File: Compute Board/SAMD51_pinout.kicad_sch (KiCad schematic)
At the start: 10 parts, among them U11 SAMD51

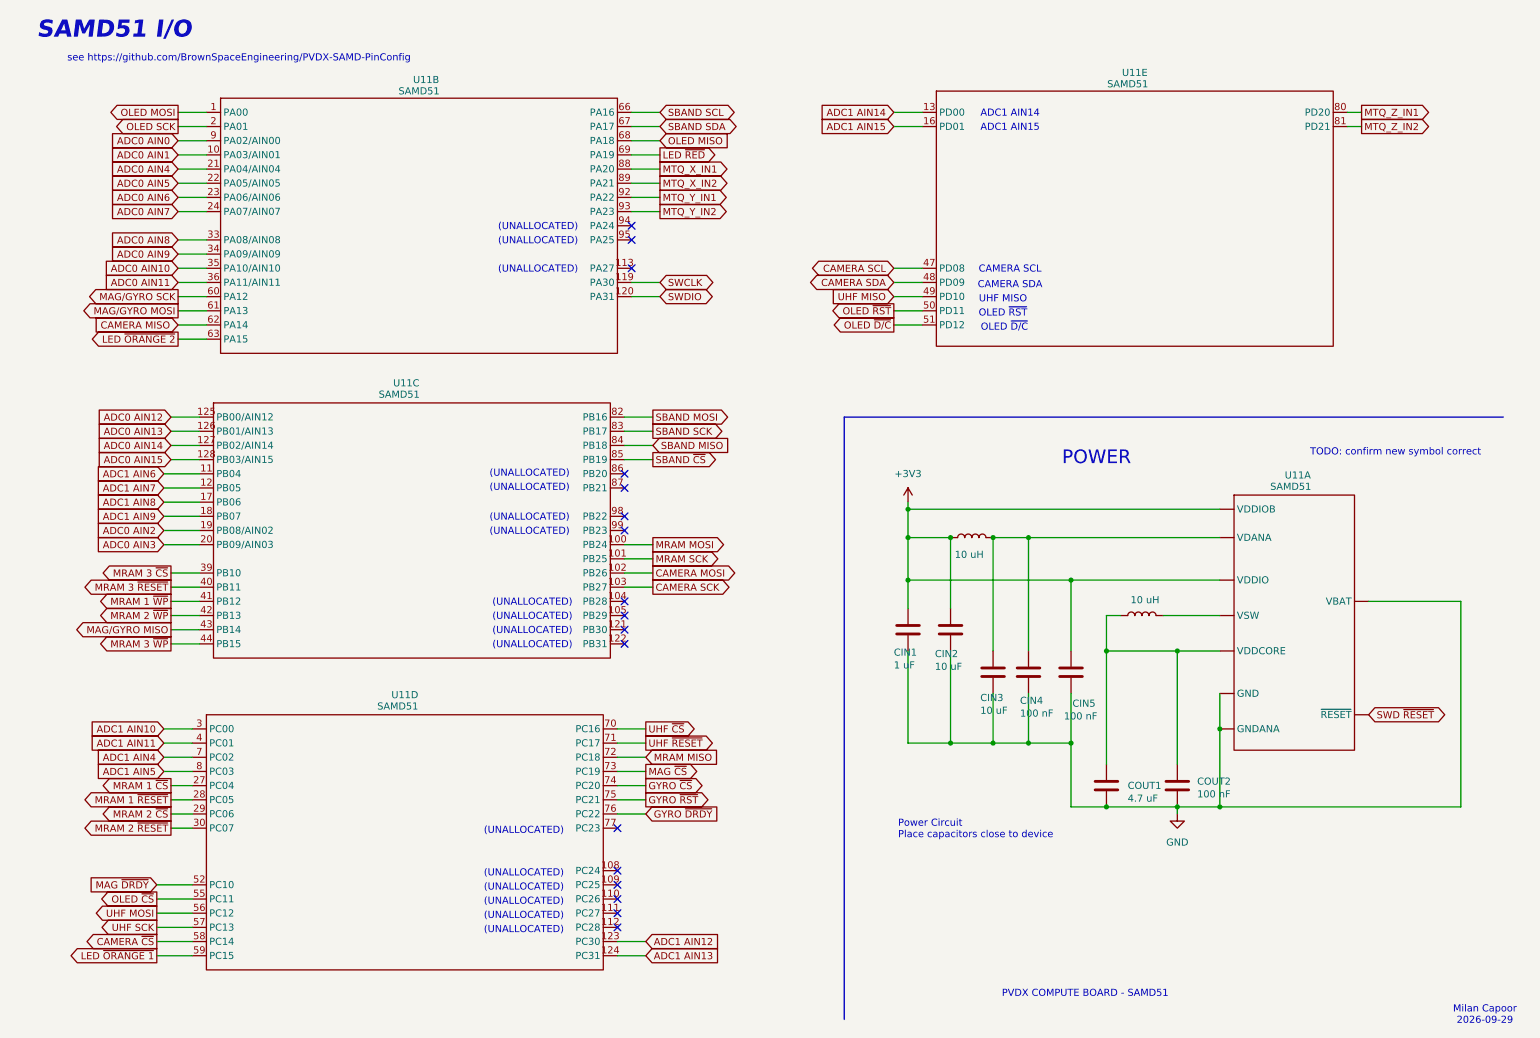
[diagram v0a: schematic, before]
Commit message: Push layout-ready schematics and partial routing
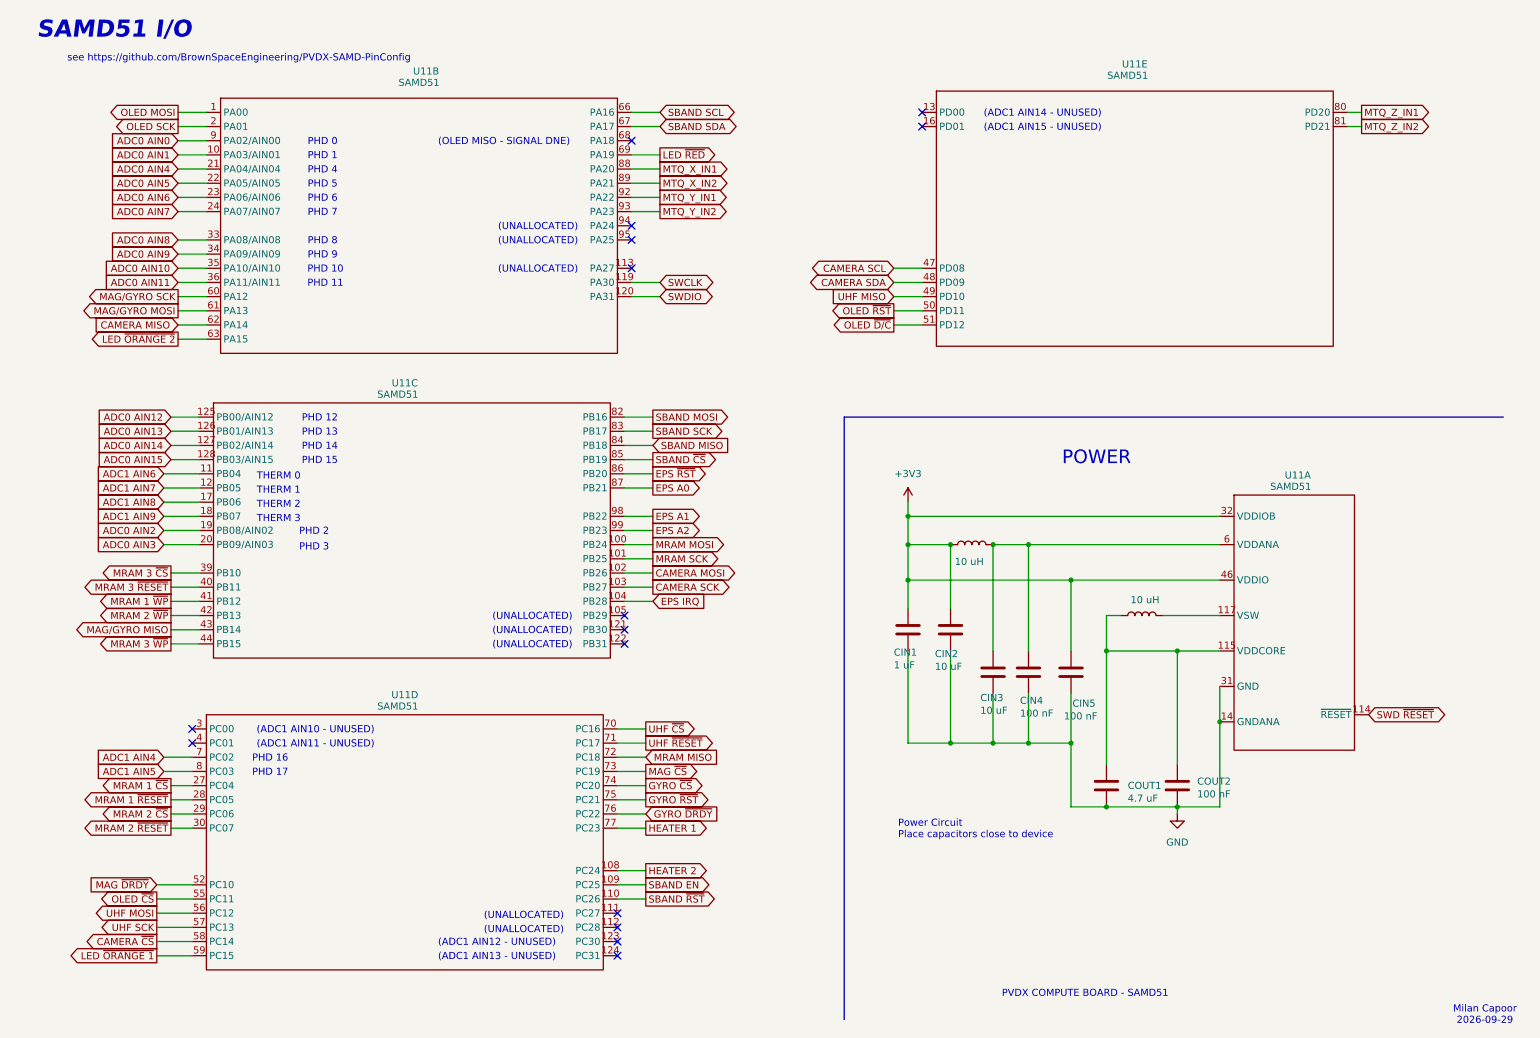
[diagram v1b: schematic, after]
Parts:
- CIN1, CIN2, CIN3, CIN4, CIN5, COUT1, COUT2: footprint Capacitor_SMD:C_0402_1005Metric -> Capacitor_SMD:C_0603_1608Metric
- L3, L4: footprint Inductor_SMD:L_0402_1005Metric -> Inductor_SMD:L_0603_1608Metric
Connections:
- net +3V3: now also U11.107 (VDDIO), U11.118 (VDDIO), U11.32 (VDDIOB), U11.37 (VDDIOB), U11.46 (VDDIO), U11.54 (VDDIO), U11.65 (VDDIO), U11.79 (VDDIO), U11.91 (VDDIO), U11.97 (VDDIO); no longer U11. (~{RESET})
- net GND: now also U11.106 (GND), U11.14 (GNDANA), U11.25 (GNDANA), U11.31 (GND), U11.38 (GND), U11.45 (GND), U11.5 (GND), U11.53 (GND), U11.64 (GND), U11.78 (GND), U11.90 (GND), U11.96 (GND); no longer U11. (~{RESET})
- net SWD ~{RESET}: now also U11.114 (~{RESET}); no longer U11. (~{RESET})
- net VDDANA: now reaches CIN3.1, CIN4.1, L3.2
- net VDDANA: now also U11.15 (VDDANA), U11.26 (VDDANA), U11.6 (VDDANA); no longer U11. (~{RESET})
- net at COUT1.1, COUT2.1, L4.1: now also U11.115 (VDDCORE); no longer U11. (~{RESET})
- net at L4.2: now also U11.117 (VSW); no longer U11. (~{RESET})
- net HEATER 2: now reaches U11.108 (PC24)
- net SBAND EN: now reaches U11.109 (PC25)
- net SBAND ~{RST}: now reaches U11.110 (PC26)
- net HEATER 1: now reaches U11.77 (PC23)
- net EPS IRQ: now reaches U11.104 (PB28)
- net EPS ~{RST}: now reaches U11.86 (PB20)
- net EPS A0: now reaches U11.87 (PB21)
- net EPS A1: now reaches U11.98 (PB22)
- net EPS A2: now reaches U11.99 (PB23)
- net ADC1 AIN10: no longer names the net of U11.3 (PC00)
- net ADC1 AIN11: no longer names the net of U11.4 (PC01)
- net ADC1 AIN12: no longer names the net of U11.123 (PC30)
- net ADC1 AIN13: no longer names the net of U11.124 (PC31)
- net ADC1 AIN14: no longer names the net of U11.13 (PD00)
- net ADC1 AIN15: no longer names the net of U11.16 (PD01)
- net OLED MISO: no longer names the net of U11.68 (PA18)
- no-connect marks 17 -> 15
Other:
- note added: "(ADC1 AIN10 - UNUSED)"
- note added: "(ADC1 AIN11 - UNUSED)"
- note added: "(ADC1 AIN12 - UNUSED)"
- note added: "(ADC1 AIN13 - UNUSED)"
- note added: "(ADC1 AIN14 - UNUSED)"
- note added: "(ADC1 AIN15 - UNUSED)"
- note added: "(OLED MISO - SIGNAL DNE)"
- note added: "PHD 0"
- note added: "PHD 1"
- note added: "PHD 10"
- note added: "PHD 11"
- note added: "PHD 12"
- note added: "PHD 13"
- note added: "PHD 14"
- note added: "PHD 15"
- note added: "PHD 16"
- note added: "PHD 17"
- note added: "PHD 2"
- note added: "PHD 3"
- note added: "PHD 4"
- note added: "PHD 5"
- note added: "PHD 6"
- note added: "PHD 7"
- note added: "PHD 8"
- note added: "PHD 9"
- note added: "THERM 0"
- note added: "THERM 1"
- note added: "THERM 2"
- note added: "THERM 3"
- note removed: "ADC1 AIN14"
- note removed: "ADC1 AIN15"
- note removed: "CAMERA SCL"
- note removed: "CAMERA SDA"
- note removed: "OLED ~{D/C}"
- note removed: "OLED ~{RST}"
- note removed: "TODO: confirm new symbol correct"
- note removed: "UHF MISO"

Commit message: Push finished layout minus perovskites
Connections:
- net GND: now also U11.116 (GNDIO)
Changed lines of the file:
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@@
+	)
+	(symbol
+		(lib_id "power:GND")
+		(at 256.54 134.62 90)
+		(unit 1)
+		(body_style 1)
+		(exclude_from_sim no)
+		(in_bom yes)
+		(on_board yes)
+		(in_pos_files yes)
+		(dnp no)
+		(fields_autoplaced yes)
+		(property "Reference" "#PWR065"
+			(at 262.89 134.62 0)
+			(hide yes)
+			(show_name no)
+			(do_not_autoplace no)
+			(effects
+				(font
+					(size 1.27 1.27)
+				)
+			)
+		)
+		(property "Value" "GND"
+			(at 260.35 134.6199 90)
+			(show_name no)
+			(do_not_autoplace no)
+			(effects
+				(font
+					(size 1.27 1.27)
+				)
+				(justify right)
+			)
+		)
+		(property "Footprint" ""
+			(at 256.54 134.62 0)
+			(hide yes)
+			(show_name no)
+			(do_not_autoplace no)
+			(effects
+				(font
+					(size 1.27 1.27)
+				)
+			)
+		)
+		(property "Datasheet" ""
+			(at 256.54 134.62 0)
+			(hide yes)
+			(show_name no)
+			(do_not_autoplace no)
+			(effects
+				(font
+					(size 1.27 1.27)
+				)
+			)
+		)
+		(property "Description" "Power symbol creates a global label with name \"GND\" , ground"
+			(at 256.54 134.62 0)
+			(hide yes)
+			(show_name no)
+			(do_not_autoplace no)
+			(effects
+				(font
+					(size 1.27 1.27)
+				)
+			)
+		)
+		(pin "1"
+		)
+		(instances
+			(project "PVDX Compute Board"
+				(path "/cc5055d2-349f-4e91-a151-9a2f788b119f/ea0f2518-2951-420b-9275-c672d5183aa9"
+					(reference "#PWR065")
+					(unit 1)
+				)
+			)
+		)
 	)
 	(symbol
@@
 		(pin "117"
 		)
+		(pin "116"
+		)
 		(instances
 			(project "PVDX Compute Board"
@@
 		(pin "117"
 		)
+		(pin "116"
+		)
 		(instances
 			(project "PVDX Compute Board"
@@
 		(pin "117"
 		)
+		(pin "116"
+		)
 		(instances
 			(project "PVDX Compute Board"
@@
 		(pin "117"
 		)
+		(pin "116"
+		)
 		(instances
 			(project "PVDX Compute Board"
@@
 		(pin "117"
 		)
+		(pin "116"
+		)
 		(instances

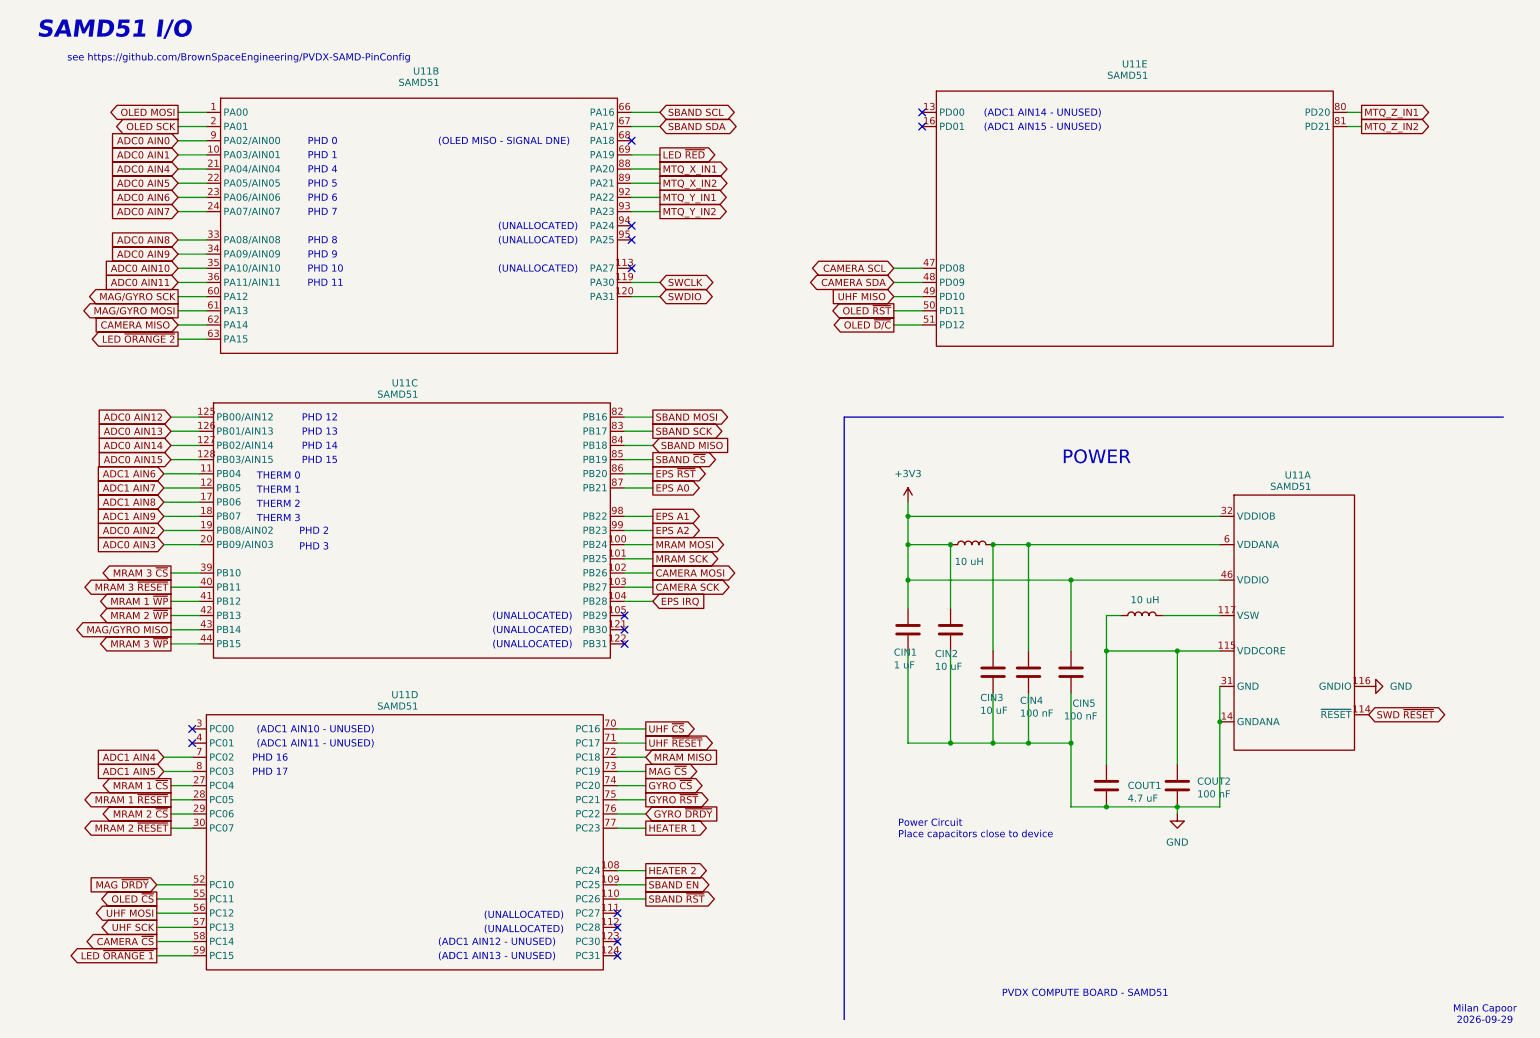
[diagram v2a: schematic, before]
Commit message: Add perovskite and magnetorquer sleep routing
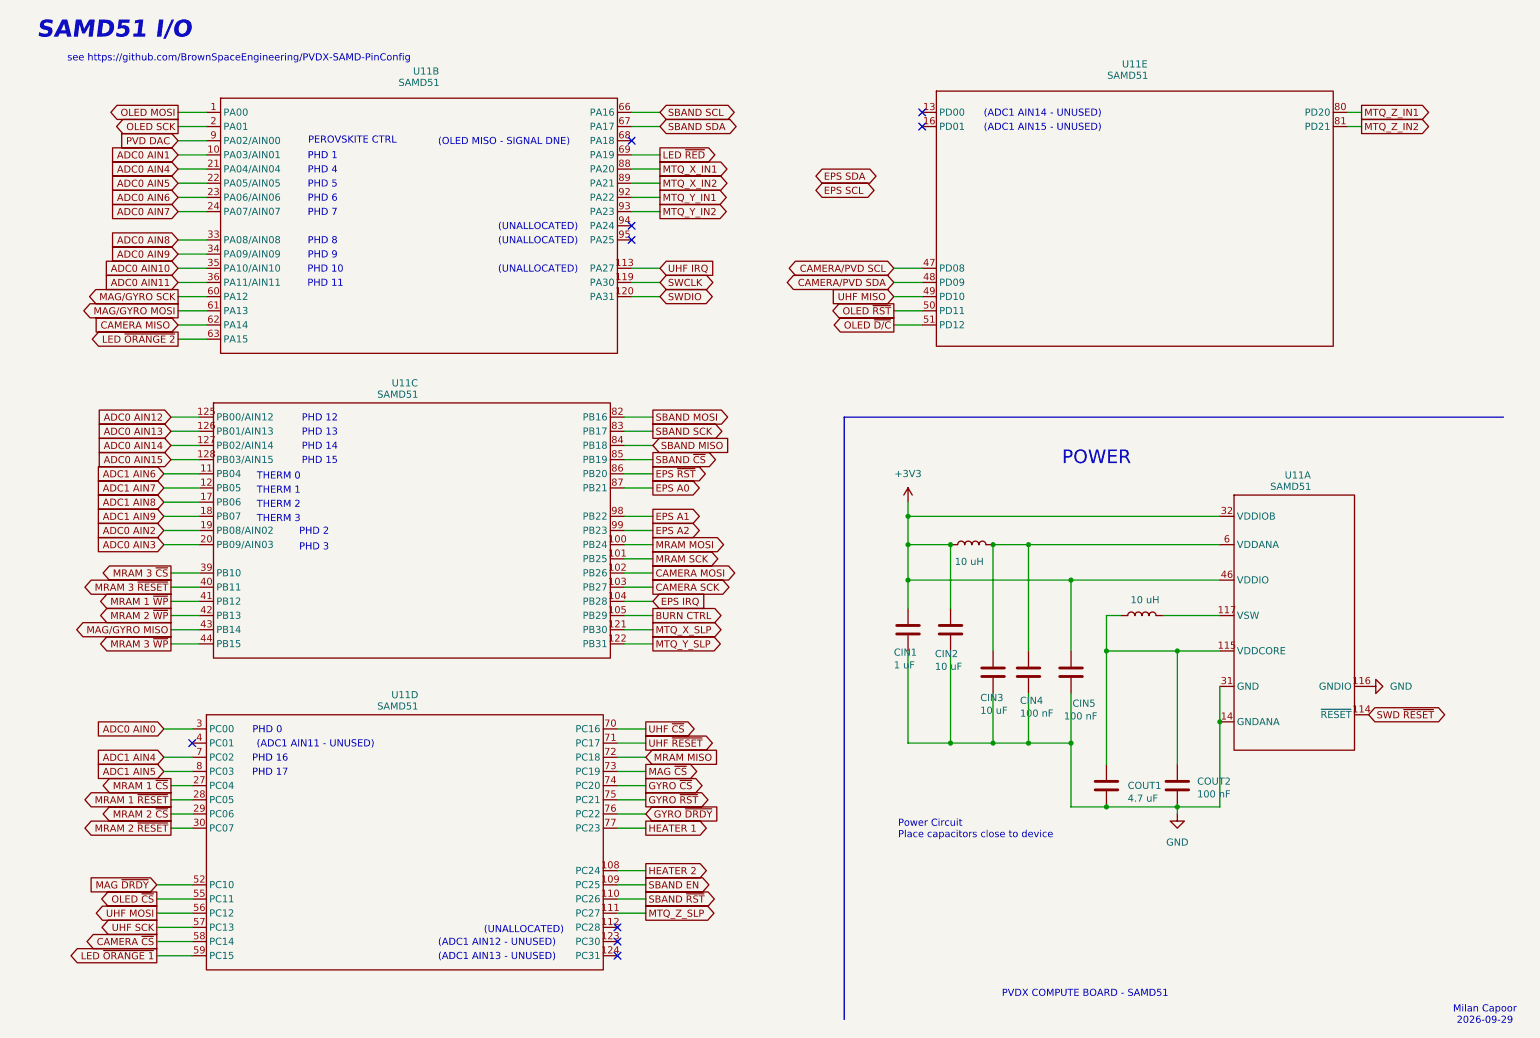
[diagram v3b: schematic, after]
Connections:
- net ADC0 AIN0: now also U11.3 (PC00); no longer U11.9 (PA02/AIN00)
- net UHF IRQ: now reaches U11.113 (PA27)
- net MTQ_Z_SLP: now reaches U11.111 (PC27)
- net BURN CTRL: now reaches U11.105 (PB29)
- net MTQ_X_SLP: now reaches U11.121 (PB30)
- net MTQ_Y_SLP: now reaches U11.122 (PB31)
- net CAMERA SCL renamed CAMERA/PVD SCL
- net CAMERA SDA renamed CAMERA/PVD SDA
- new net PVD DAC: U11.9 (PA02/AIN00)
- no-connect marks 15 -> 9
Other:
- note added: "PEROVSKITE CTRL"
- note removed: "(ADC1 AIN10 - UNUSED)"

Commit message: Finished routing
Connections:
- net CAMERA/PVD SCL renamed CAMERA/PVD/EPS SCL
- net CAMERA/PVD SDA renamed CAMERA/PVD/EPS SDA
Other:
- note removed: "(OLED MISO - SIGNAL DNE)"
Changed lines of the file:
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@@
 		)
 	)
-	(text "(OLED MISO - SIGNAL DNE)"
-		(exclude_from_sim no)
-		(at 101.6 37.084 0)
-		(effects
-			(font
-				(size 1.27 1.27)
-				(color 255 0 0 1)
-			)
-		)
-	)
 	(text "THERM 3"
 		(exclude_from_sim no)
@@
 		)
 	)
-	(global_label "EPS SDA"
+	(global_label "CAMERA{slash}PVD{slash}EPS SDA"
 		(shape bidirectional)
-		(at 157.48 43.18 0)
-		(fields_autoplaced yes)
+		(at 171.45 62.23 180)
 		(effects
 			(font
 				(size 1.27 1.27)
 			)
-			(justify left)
+			(justify right)
 		)
 		(property "Intersheetrefs" "${INTERSHEET_REFS}"
-			(at 168.6294 43.18 0)
+			(at 156.3938 60.198 0)
 			(hide yes)
 			(show_name no)
@@
 					(size 1.27 1.27)
 				)
-				(justify left)
+				(justify right)
 			)
 		)
@@
 		)
 	)
+	(global_label "CAMERA{slash}PVD{slash}EPS SCL"
+		(shape bidirectional)
+		(at 171.45 59.69 180)
+		(effects
+			(font
+				(size 1.27 1.27)
+			)
+			(justify right)
+		)
+		(property "Intersheetrefs" "${INTERSHEET_REFS}"
+			(at 156.3938 57.658 0)
+			(hide yes)
+			(show_name no)
+			(do_not_autoplace no)
+			(effects
+				(font
+					(size 1.27 1.27)
+				)
+				(justify right)
+			)
+		)
+	)
 	(global_label "SWCLK"
 		(shape bidirectional)
@@
 		)
 	)
-	(global_label "CAMERA{slash}PVD SCL"
-		(shape bidirectional)
-		(at 171.45 59.69 180)
-		(effects
-			(font
-				(size 1.27 1.27)
-			)
-			(justify right)
-		)
-		(property "Intersheetrefs" "${INTERSHEET_REFS}"
-			(at 156.3938 57.658 0)
-			(hide yes)
-			(show_name no)
-			(do_not_autoplace no)
-			(effects
-				(font
-					(size 1.27 1.27)
-				)
-				(justify right)
-			)
-		)
-	)
 	(global_label "ADC1 AIN9"
 		(shape input)
@@
 		)
 	)
-	(global_label "CAMERA{slash}PVD SDA"
-		(shape bidirectional)
-		(at 171.45 62.23 180)
-		(effects
-			(font
-				(size 1.27 1.27)
-			)
-			(justify right)
-		)
-		(property "Intersheetrefs" "${INTERSHEET_REFS}"
-			(at 156.3938 60.198 0)
-			(hide yes)
-			(show_name no)
-			(do_not_autoplace no)
-			(effects
-				(font
-					(size 1.27 1.27)
-				)
-				(justify right)
-			)
-		)
-	)
 	(global_label "MTQ_Y_IN2"
 		(shape output)
@@
 			(hide yes)
 			(show_name no)
-			(do_not_autoplace no)
-			(effects
-				(font
-					(size 1.27 1.27)
-				)
-				(justify left)
-			)
-		)
-	)
-	(global_label "EPS SCL"
-		(shape bidirectional)
-		(at 157.48 45.72 0)
-		(fields_autoplaced yes)
-		(effects
-			(font
-				(size 1.27 1.27)
-			)
-			(justify left)
-		)
-		(property "Intersheetrefs" "${INTERSHEET_REFS}"
-			(at 168.5689 45.72 0)
-			(hide yes)
-			(show_name no)
